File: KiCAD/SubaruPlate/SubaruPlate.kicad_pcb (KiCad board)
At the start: 2 copper layers, 140 x 140 mm, 38 parts, among them J1 DF51A-4P-2DSA, Q1 NMOS, U1 LPS28DFW, U2 NCV8114BSN330T1G, U3 MCP2515-xSO, U4 MCP2562-E-SN, U5 XIAO-RP2040-DIP, Y1 8MHz

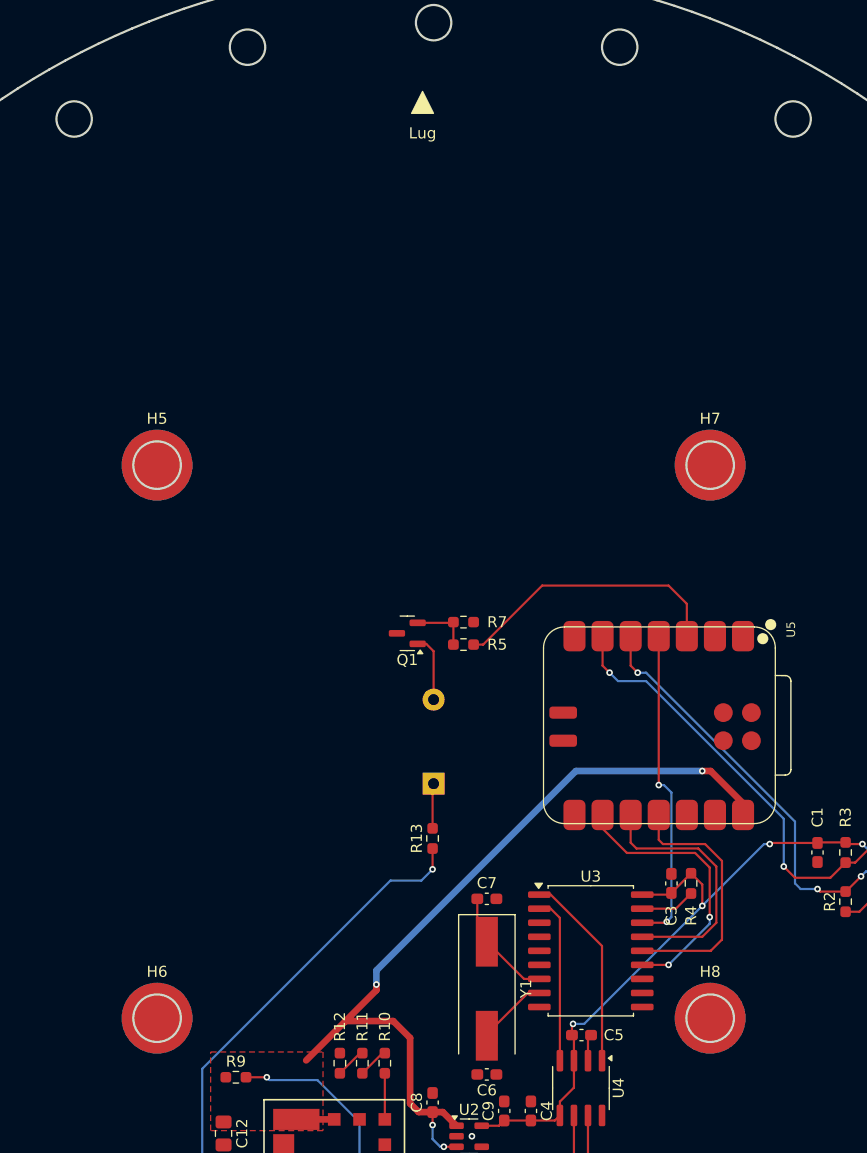
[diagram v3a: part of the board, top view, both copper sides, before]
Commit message: 取付穴位置を変更
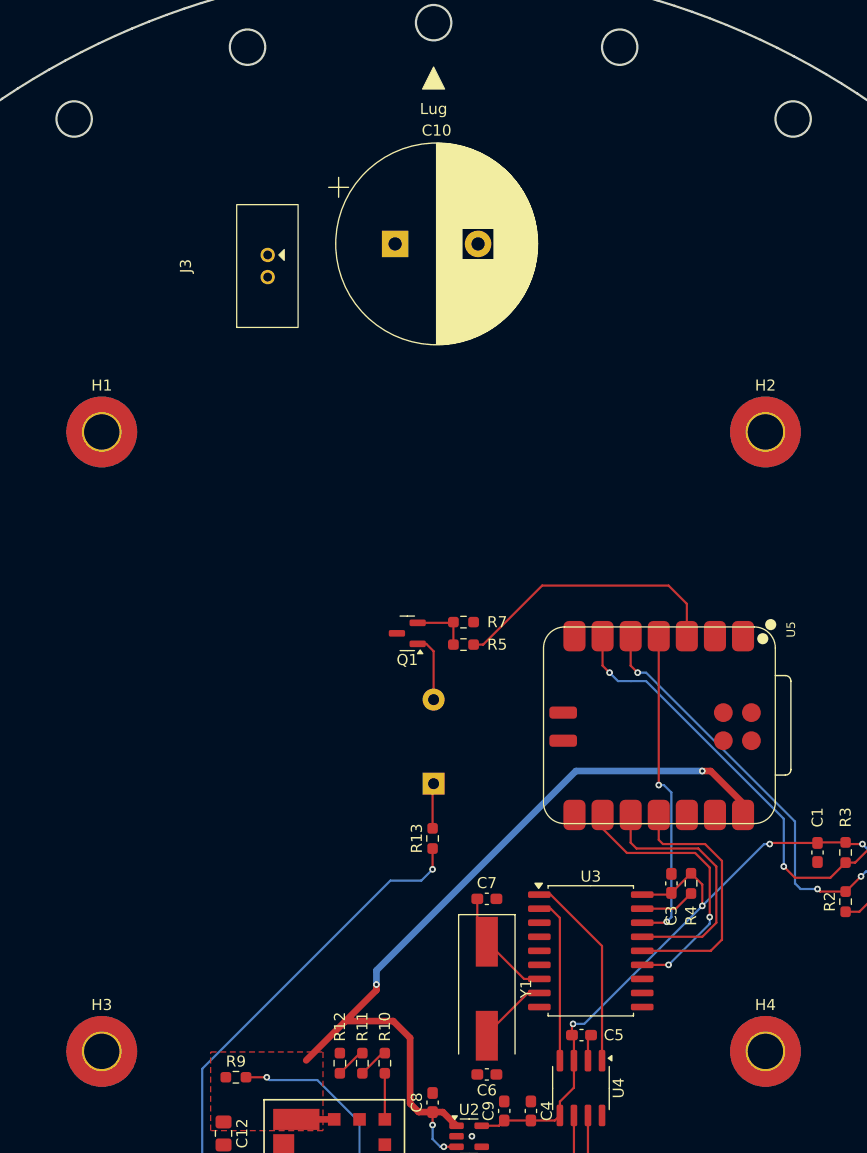
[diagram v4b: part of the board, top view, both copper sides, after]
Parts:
- removed H5, H6, H7, H8: MountingHole_Pad, MountingHole:MountingHole_3.2mm_M3_Pad_TopBottom
- added C10: 2200uF, Capacitor_THT:CP_Radial_D18.0mm_P7.50mm, F.Cu at (146.5, 55.0)
- added H1: MountingHole, MountingHole:MountingHole_3.2mm_M3_Pad_TopBottom, F.Cu at (120.0, 72.0)
- added H2: MountingHole, MountingHole:MountingHole_3.2mm_M3_Pad_TopBottom, F.Cu at (180.0, 72.0)
- added H3: MountingHole, MountingHole:MountingHole_3.2mm_M3_Pad_TopBottom, F.Cu at (120.0, 128.0)
- added H4: MountingHole, MountingHole:MountingHole_3.2mm_M3_Pad_TopBottom, F.Cu at (180.0, 128.0)
- added J3: Power, TSRP_Connector_Hirose:DF51A-2P-2DSA, F.Cu at (137.6, 57.0)
- C11: value 22u -> 22uF
- C12: value 10u -> 10uF
- C8, C9: value 1u -> 1uF
- R1, R2, R3, R4: value 10K -> 10kR
- R10: value 1k 0.1% -> 1kR 0.1%
- R11: value 330 0.1% -> 330R 0.1%
- R12: value 10 0.1% -> 10R 0.1%
- R13: value 600 -> 600R
- R5: value 750 -> 750R
- R6: value 120 -> 120R
- R7: value 10k -> 10kR
- R8: value 20k -> 20kR
- R9: value 100k -> 100kR
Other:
- outline, holes or cut-outs redrawn

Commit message: ガバーデータ生成
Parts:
- added C13: 0.1uF, Capacitor_SMD:C_0603_1608Metric_Pad1.08x0.95mm_HandSolder, F.Cu at (191.9, 95.2)
- added C14: 10uF, Capacitor_SMD:C_0603_1608Metric_Pad1.08x0.95mm_HandSolder, F.Cu at (191.9, 93.5)
- added D1: D, Diode_SMD:D_SMA, F.Cu at (148.4, 150.8)
- added G***: LOGO, LOGO, F.Cu at (150.0, 77.5)
- added G***: LOGO, LOGO, B.Cu at (133.5, 135.2)
- added G***: LOGO, LOGO, B.Cu at (138.4, 83.1)
- added G***: LOGO, LOGO, B.Cu at (127.8, 100.5)
- added G***: LOGO, LOGO, B.Cu at (135.2, 148.4)
- added G***: LOGO, LOGO, B.Cu at (141.1, 113.5)
- added G***: LOGO, LOGO, B.Cu at (142.5, 124.5)
- added G***: LOGO, LOGO, B.Cu at (171.5, 100.4)
- added G***: LOGO, LOGO, B.Cu at (141.4, 56.6)
- added G***: LOGO, LOGO, B.Cu at (164.7, 148.4)
- added G***: LOGO, LOGO, B.Cu at (150.1, 71.0)
- added G***: LOGO, LOGO, B.Cu at (170.3, 84.1)
- added G***: LOGO, LOGO, B.Cu at (162.2, 135.0)
- added G***: LOGO, LOGO, B.Cu at (173.5, 115.9)
- added R14: 10kR, Resistor_SMD:R_0603_1608Metric_Pad0.98x0.95mm_HandSolder, F.Cu at (187.2, 91.7)
- added R15: 10kR, Resistor_SMD:R_0603_1608Metric_Pad0.98x0.95mm_HandSolder, F.Cu at (191.5, 85.3)
- added R16: 10kR, Resistor_SMD:R_0603_1608Metric_Pad0.98x0.95mm_HandSolder, F.Cu at (187.2, 87.6)
- added U6: LPS28DFW, TSRP_IC:CCLGA-7L, B.Cu at (192.0, 89.5)
- J3: value Power -> DF51A-2P-2DSA
- U5: footprint Seeed_XIAO:XIAO-RP2040-SMD -> TSRP_Seeed_XIAO:XIAO-RP2040-SMD
- moved J3 39.4 mm to (176.5, 62.7), turned to 0 degrees
- moved C1 9.77 mm to (191.5, 117.0), turned to 0 degrees
- moved C10 8.90 mm to (155.4, 55.5)
- moved R9 3.77 mm to (135.0, 127.9), turned to 90 degrees
- moved J1 1.66 mm to (163.0, 141.0)
- moved R6 1.53 mm to (163.4, 137.7)
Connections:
- net Net-(J3-Pin_1) renamed /Power/Capacitor OUT
- net Net-(J3-Pin_2) renamed /Power/Capacitor IN
- C11 pad 1: +12V -> VIN(12V)
- MD2 pad 2: +12V -> VIN(12V)
- R13 pad 1: +12V -> VIN(12V)
- R8 pad 1: +12V -> VIN(12V)
- U5 pad 1: SPI_CS -> unconnected-(U5-GPIO26/ADC0/A0-Pad1)
- U5 pad 2: Servo_PWM -> unconnected-(U5-GPIO27/ADC1/A1-Pad2)
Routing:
- net +12V: track 81.2 -> 16.0 mm, vias 2 -> 0
- net VIN(12V): track 0.00 -> 55.1 mm, vias 0 -> 2
- net +3.3V: track 69.4 -> 102.5 mm, vias 6 -> 9
- net I2C_SCL: track 43.7 -> 75.7 mm, vias 3 -> 5
- net I2C_SDA: track 37.9 -> 62.1 mm, vias 3 -> 5
- net /Power/Capacitor IN: track 0.00 -> 23.4 mm
- net /Power/Capacitor OUT: track 0.00 -> 18.0 mm
- net P.G._OKL-T/6-W12N-C: track 20.8 -> 35.3 mm
- net CAN_H: track 5.57 -> 10.9 mm
- net CAN_L: track 5.53 -> 10.6 mm
- net Net-(U6-SA0): track 0.00 -> 3.64 mm, vias 0 -> 1
- net GND: track 3.62 -> 5.44 mm, vias 5 -> 6
- net +5V: track 79.6 -> 81.3 mm
- net OSC1: track 9.07 -> 10.3 mm
- added copper zone on F.Cu, net VIN(12V)
- removed copper zone on F.Cu, net +12V
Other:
- outline, holes or cut-outs redrawn
- board text added: "3 ~ 6 mm"
- board text added: "Cable Diameter"
- board text added: "RM10L-6B"
- board text added: "SUBARU"
- board text added: "Subaru Plate Build-1"
- board text added: "Tokai Student Rocket Project"
- board text added: "V1.3"

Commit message: Build-2完成．発注．
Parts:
- removed BZ1: Buzzer, Buzzer_Beeper:Buzzer_12x9.5RM7.6
- removed C10: 2200uF, Capacitor_THT:CP_Radial_D18.0mm_P7.50mm
- removed C11: 22uF, Capacitor_SMD:C_0805_2012Metric_Pad1.18x1.45mm_HandSolder
- removed C12: 10uF, Capacitor_SMD:C_0805_2012Metric_Pad1.18x1.45mm_HandSolder
- removed C3, C4, C5: 0.1uF, Capacitor_SMD:C_0603_1608Metric_Pad1.08x0.95mm_HandSolder
- removed C6, C7: 15pF, Capacitor_SMD:C_0603_1608Metric_Pad1.08x0.95mm_HandSolder
- removed C8, C9: 1uF, Capacitor_SMD:C_0603_1608Metric_Pad1.08x0.95mm_HandSolder
- removed D1: D, Diode_SMD:D_SMA
- removed J3: DF51A-2P-2DSA, TSRP_Connector_Hirose:DF51A-2P-2DSA
- removed MD2: OKL-T_6-W12N-C, TSRP_IC:MURATA_OKL-T-6-W12N-C_0
- removed Q1: NMOS, Package_TO_SOT_SMD:SOT-23
- removed R10: 1kR 0.1%, Resistor_SMD:R_0603_1608Metric_Pad0.98x0.95mm_HandSolder
- removed R11: 330R 0.1%, Resistor_SMD:R_0603_1608Metric_Pad0.98x0.95mm_HandSolder
- removed R12: 10R 0.1%, Resistor_SMD:R_0603_1608Metric_Pad0.98x0.95mm_HandSolder
- removed R13: 600R, Resistor_SMD:R_0603_1608Metric_Pad0.98x0.95mm_HandSolder
- removed R15, R4, R7: 10kR, Resistor_SMD:R_0603_1608Metric_Pad0.98x0.95mm_HandSolder
- removed R5: 750R, Resistor_SMD:R_0603_1608Metric_Pad0.98x0.95mm_HandSolder
- removed R6: 120R, Resistor_SMD:R_0603_1608Metric_Pad0.98x0.95mm_HandSolder
- removed R8: 20kR, Resistor_SMD:R_0603_1608Metric_Pad0.98x0.95mm_HandSolder
- removed R9: 100kR, Resistor_SMD:R_0603_1608Metric_Pad0.98x0.95mm_HandSolder
- removed U2: NCV8114BSN330T1G, Package_TO_SOT_SMD:TSOT-23-5
- removed U3: MCP2515-xSO, Package_SO:SOIC-18W_7.5x11.6mm_P1.27mm
- removed U4: MCP2562-E-SN, Package_SO:SOIC-8_3.9x4.9mm_P1.27mm
- removed U5: XIAO-RP2040-DIP, TSRP_Seeed_XIAO:XIAO-RP2040-SMD
- removed Y1: 8MHz, Crystal:Crystal_SMD_HC49-SD
- J1: value DF51A-4P-2DSA -> Wire_Soldering; footprint TSRP_Connector_Hirose:DF51A-4P-2DSA -> Connector_PinHeader_1.27mm:PinHeader_1x04_P1.27mm_Vertical
- moved J1 75.8 mm to (151.9, 66.0), turned to -90 degrees
- moved R2 65.5 mm to (136.7, 72.8), turned to 0 degrees
- moved U1 62.6 mm to (139.5, 77.2), turned to 90 degrees
- moved C1 61.8 mm to (146.0, 75.2), turned to -90 degrees
- moved C2 59.5 mm to (147.7, 75.2), turned to -90 degrees
- moved R3 59.2 mm to (141.2, 72.8), turned to 180 degrees
- moved R1 56.7 mm to (143.7, 77.1), turned to -90 degrees
- moved G*** 55.2 mm to (191.9, 78.7)
- moved C13 40.0 mm to (156.0, 77.4), turned to -90 degrees
- moved C14 37.8 mm to (157.7, 77.4), turned to -90 degrees
- moved R14 33.6 mm to (159.4, 72.7), turned to 0 degrees
- moved G*** 32.8 mm to (108.7, 113.7)
- moved U6 32.6 mm to (161.7, 77.5), turned to 90 degrees
- moved R16 27.8 mm to (163.6, 72.7), turned to 180 degrees
- moved G*** 27.0 mm to (195.1, 113.5)
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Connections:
- H1 pad 1: (no net) -> GND
- H2 pad 1: (no net) -> GND
- H3 pad 1: (no net) -> GND
- H4 pad 1: (no net) -> GND
- J1 pad 2: +12V -> +3.3V
- J1 pad 3: CAN_L -> I2C_SDA
- J1 pad 4: CAN_H -> I2C_SCL
- U6 pad 2: Net-(U6-SA0) -> +3.3V
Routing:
- net +5V: track 81.3 -> 0.00 mm, vias 4 -> 0
- net VIN(12V): track 55.1 -> 0.00 mm, vias 2 -> 0
- net +3.3V: track 102.5 -> 54.4 mm, vias 9 -> 6
- net P.G._OKL-T/6-W12N-C: track 35.3 -> 0.00 mm, vias 2 -> 0
- net SPI_CS_MCP2515: track 29.0 -> 0.00 mm, vias 2 -> 0
- net I2C_SCL: track 75.7 -> 47.6 mm, vias 5 -> 4
- net SPI_SCK: track 25.1 -> 0.00 mm, vias 2 -> 0
- net Buzzer: track 25.1 -> 0.00 mm
- net SPI_MOSI: track 23.5 -> 0.00 mm
- net SPI_MISO: track 23.5 -> 0.00 mm
- net /Power/Capacitor IN: track 23.4 -> 0.00 mm
- net I2C_SDA: track 62.1 -> 39.9 mm, vias 5 -> 4
- net CAN_TX: track 18.0 -> 0.00 mm
- net /Power/Capacitor OUT: track 18.0 -> 0.00 mm
- net +12V: track 16.0 -> 0.00 mm
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- removed copper zone on F.Cu, net +5V
- removed copper zone on F.Cu, net VIN(12V)
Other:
- outline, holes or cut-outs redrawn
- board text added: "0x5C"
- board text added: "0x5D"
- board text added: "3.3V"
- board text added: "Address"
- board text added: "GND"
- board text added: "I2C"
- board text added: "SCL"
- board text added: "SDA"
- board text added: "Subaru Plate Build-2"
- board text removed: "Subaru Plate Build-1"
